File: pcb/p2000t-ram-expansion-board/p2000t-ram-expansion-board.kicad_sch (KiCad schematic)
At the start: 22 parts, among them J1 EXTENSION BOARD, J2 POWER, U1 74HC04, U10 74HC32, U2 CY62256-70PC, U3 74HC32, U4 CY62256-70PC, U5 74HC688, U6 74HC04, U7 74HC08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

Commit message: Revising design
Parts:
- removed C10: 0.1uF, symbol Device:C
- removed U1, U6: 74HC04, Package_DIP:DIP-14_W7.62mm_Socket, symbol 74xx:74HC04
- removed U10, U3: 74HC32, Package_DIP:DIP-14_W7.62mm_Socket, symbol 74xx:74LS32
- removed U7, U9: 74HC08, Package_DIP:DIP-14_W7.62mm_Socket, symbol 74xx:74LS08
- added U2, U5: 74HC00, Package_DIP:DIP-14_W7.62mm_Socket, symbol 74xx:74HC00
- added U6: 74HC32, Package_DIP:DIP-14_W7.62mm_Socket, symbol 74xx:74LS32
- added U8: 74LHC157, Package_DIP:DIP-16_W7.62mm_Socket, symbol 74xx:74LS157
- C1, C2, C6: footprint (none) -> Capacitor_THT:C_Disc_D5.0mm_W2.5mm_P5.00mm
- C3: renamed from C9; footprint (none) -> Capacitor_THT:C_Disc_D5.0mm_W2.5mm_P5.00mm
- C4: renamed from C3; footprint (none) -> Capacitor_THT:CP_Radial_D6.3mm_P2.50mm
- C5: renamed from C4; footprint (none) -> Capacitor_THT:C_Disc_D5.0mm_W2.5mm_P5.00mm
- C7: renamed from C8; footprint (none) -> Capacitor_THT:C_Disc_D5.0mm_W2.5mm_P5.00mm
- C8: renamed from C5; footprint (none) -> Capacitor_THT:C_Disc_D5.0mm_W2.5mm_P5.00mm
- C9: renamed from C7; footprint (none) -> Capacitor_THT:C_Disc_D5.0mm_W2.5mm_P5.00mm
- J1: value EXTENSION BOARD -> EXPANSION BOARD; footprint Connector_PinSocket_2.54mm:PinSocket_2x20_P2.54mm_Horizontal -> Connector_PinHeader_2.54mm:PinHeader_2x20_P2.54mm_Horizontal
- J2: footprint (none) -> Connector_PinHeader_2.54mm:PinHeader_1x02_P2.54mm_Vertical
- renumbered U2 to U1, U4 to U3, U5 to U4, U8 to U7
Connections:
- net +5V: now also U2.14 (VCC), U5.14 (VCC), U6.14 (VCC), U8.16 (VCC), U8.6 (I1b)
- net A0: now also J1.12 (Pin_12); no longer J1.11 (Pin_11)
- net A1: now also J1.11 (Pin_11); no longer J1.12 (Pin_12)
- net A10: now also J1.22 (Pin_22); no longer J1.21 (Pin_21)
- net A11: now also J1.21 (Pin_21); no longer J1.22 (Pin_22)
- net A12: now also J1.24 (Pin_24); no longer J1.23 (Pin_23)
- net A13: now also J1.23 (Pin_23), U8.2 (I0a); no longer J1.24 (Pin_24)
- net A14: now also J1.26 (Pin_26), U5.10, U5.2, U5.9, U8.1 (S); no longer J1.25 (Pin_25)
- net A2: now also J1.14 (Pin_14); no longer J1.13 (Pin_13)
- net A3: now also J1.13 (Pin_13); no longer J1.14 (Pin_14)
- net A4: now also J1.16 (Pin_16); no longer J1.15 (Pin_15)
- net A5: now also J1.15 (Pin_15); no longer J1.16 (Pin_16)
- net A6: now also J1.18 (Pin_18); no longer J1.17 (Pin_17)
- net A7: now also J1.17 (Pin_17); no longer J1.18 (Pin_18)
- net A8: now also J1.20 (Pin_20); no longer J1.19 (Pin_19)
- net A9: now also J1.19 (Pin_19); no longer J1.20 (Pin_20)
- net D0: now also J1.4 (Pin_4); no longer J1.3 (Pin_3)
- net D1: now also J1.3 (Pin_3); no longer J1.4 (Pin_4)
- net D2: now also J1.6 (Pin_6); no longer J1.5 (Pin_5)
- net D3: now also J1.5 (Pin_5), U7.11 (D3); no longer J1.6 (Pin_6)
- net D4: now also J1.8 (Pin_8); no longer J1.7 (Pin_7)
- net D5: now also J1.7 (Pin_7); no longer J1.8 (Pin_8)
- net D6: now also J1.10 (Pin_10); no longer J1.9 (Pin_9)
- net D7: now also J1.9 (Pin_9); no longer J1.10 (Pin_10)
- net GND: now also J1.2 (Pin_2), U2.7 (GND), U5.7 (GND), U6.7 (GND), U8.15 (E), U8.5 (I0b), U8.8 (GND); no longer U7.11 (D3)
- net RAMS2: now also J1.25 (Pin_25), U2.13; no longer J1.26 (Pin_26)
- net S0: now also U8.10 (I1c), U8.11 (I0c), U8.3 (I1a)
- net S1: now also U6.9
- net S2: now also U6.10, U8.13 (I1d), U8.14 (I0d)
- net ~{CS1}: now also U1.20 (~{CS}), U6.11
- net ~{IORQ}: now also J1.32 (Pin_32); no longer J1.31 (Pin_31)
- net ~{MRQ}: now also J1.28 (Pin_28), U2.10, U2.9; no longer J1.27 (Pin_27)
- net ~{RD}: now also J1.27 (Pin_27); no longer J1.28 (Pin_28)
- net ~{RES}: now also J1.33 (Pin_33), U2.1, U2.2; no longer J1.34 (Pin_34)
- net ~{WR}: now also J1.29 (Pin_29), U2.4, U2.5; no longer J1.30 (Pin_30)
- net ~{CS2}: now reaches U3.20 (~{CS})
- net ~{CS2}: now also U6.3
- net WR: now reaches U7.7 (Cp)
- net WR: now also U2.6
- net RES: now reaches U7.15 (Mr)
- net RES: now also U2.3
- net A13P renamed A13_1
- net A13_1: now also U8.4 (Za); no longer U3.26 (A13)
- net A14P renamed A14_1
- net A14_1: now also U8.7 (Zb); no longer U3.1 (A14)
- new net: U2.12, U2.8
- new net: U5.1, U5.4, U5.5, U6.8
- new net: U5.6, U6.4
- new net: U5.11, U6.12
- new net: U5.8, U6.5
- new net: U5.12, U5.13, U6.6
- new net: U5.3, U6.1
- new net A13_2: U3.26 (A13), U8.9 (Zc)
- new net A14_2: U3.1 (A14), U8.12 (Zd)
- new net ~{REN}: U2.11, U6.13, U6.2
- no-connect marks 15 -> 11
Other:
- note added: "Truth table CS1\ CS2\ A13 A14 S0 S1 S2 A13_1 A14_1 A13_2 A14_2 0 1 0 0 x x x 0 0 x x 0 1 1 0 x x x 1 0 x x 0 1 x 1 0 x x 0 1 x x #00 0 1 x 1 1 x x 1 1 x x #01 1 0 x 1 0 1 0 x x 0 0 #02 1 0 x 1 1 1 0 x x 1 0 #03 1 0 x 1 0 0 1 x x 0 1 #04 1 0 x 1 1 0 1 x x 1 1 #05"
- note added: "Whether one of the two RAM chips should be set active"
- note removed: "L"
- moved on the sheet: C1, C2, C3, C4, C5, C6, C7, C9, J2, U1, U3

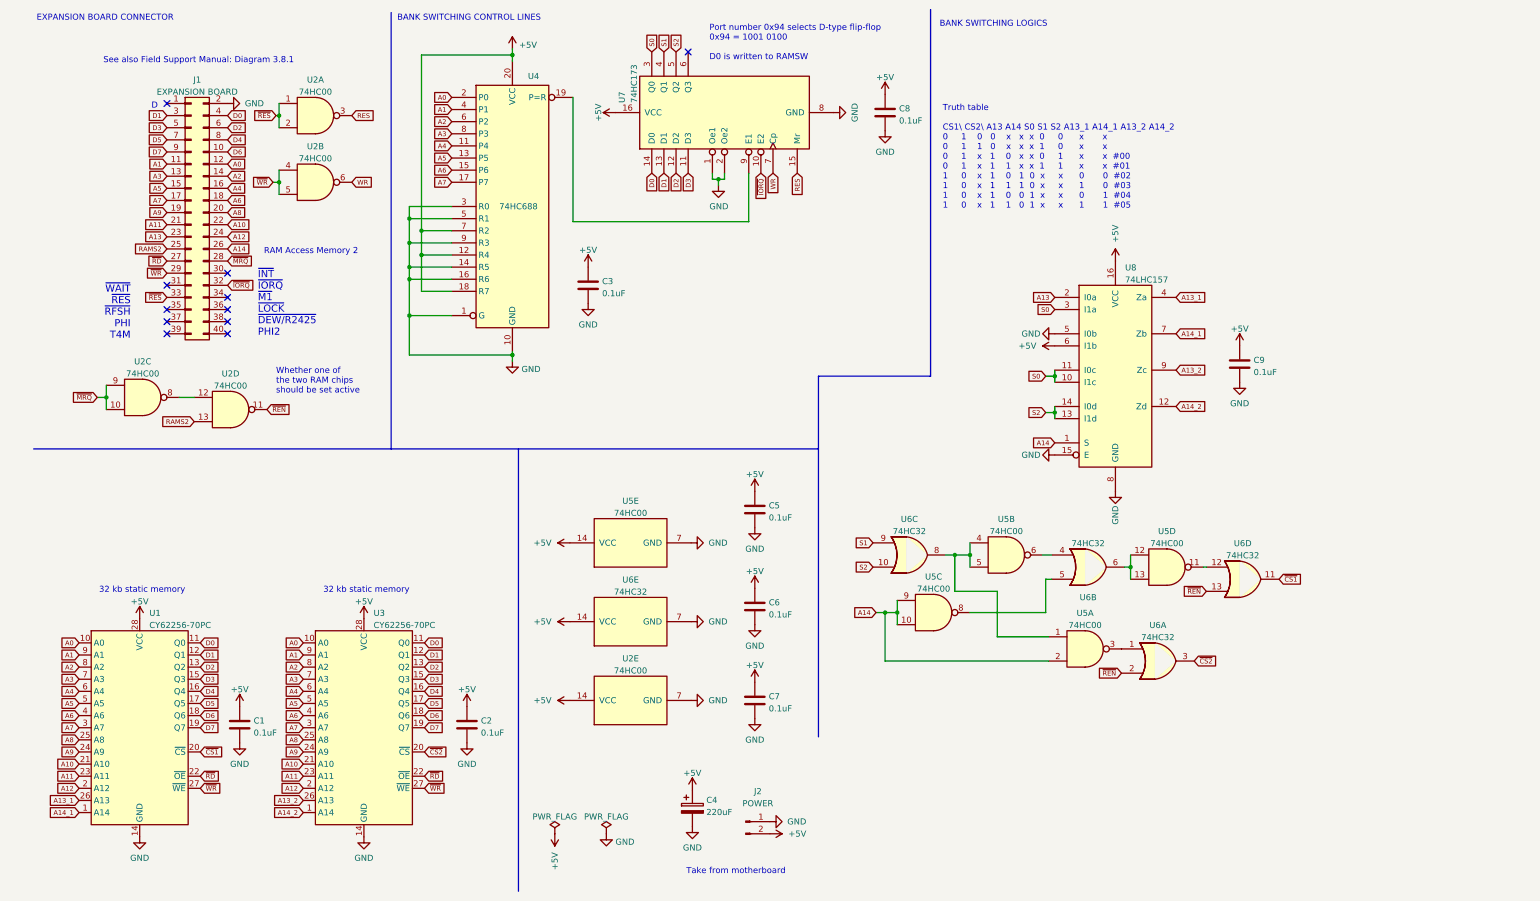
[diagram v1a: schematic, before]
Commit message: Adding reverse polarity diode and silk screen comments
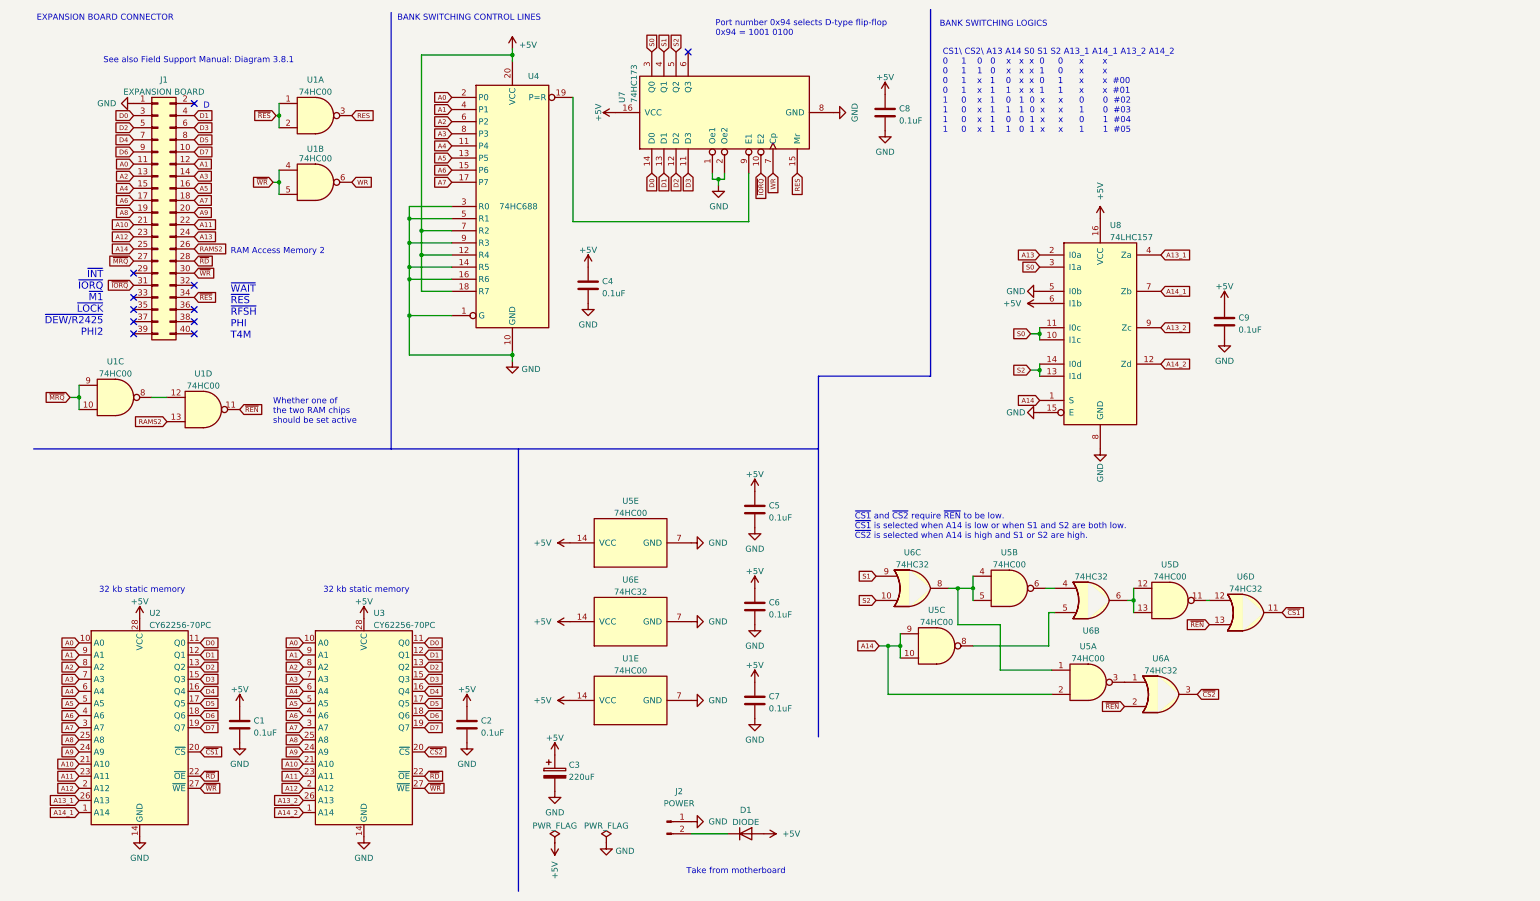
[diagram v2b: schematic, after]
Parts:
- added D1: DIODE, Diode_THT:D_DO-35_SOD27_P7.62mm_Horizontal, symbol Simulation_SPICE:DIODE
- J1: footprint Connector_PinHeader_2.54mm:PinHeader_2x20_P2.54mm_Horizontal -> Connector_PinHeader_2.54mm:PinHeader_2x20_P2.54mm_Vertical
- U2: renamed from U1; footprint Package_DIP:DIP-28_W15.24mm -> Package_DIP:DIP-28_W15.24mm_Socket
- U3: footprint Package_DIP:DIP-28_W15.24mm -> Package_DIP:DIP-28_W15.24mm_Socket
- renumbered C4 to C3, C3 to C4, U2 to U1
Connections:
- net +5V: now also D1.1 (A); no longer J2.2 (Pin_2)
- net A0: now also J1.11 (Pin_11); no longer J1.12 (Pin_12)
- net A1: now also J1.12 (Pin_12); no longer J1.11 (Pin_11)
- net A10: now also J1.21 (Pin_21); no longer J1.22 (Pin_22)
- net A11: now also J1.22 (Pin_22); no longer J1.21 (Pin_21)
- net A12: now also J1.23 (Pin_23); no longer J1.24 (Pin_24)
- net A13: now also J1.24 (Pin_24); no longer J1.23 (Pin_23)
- net A14: now also J1.25 (Pin_25); no longer J1.26 (Pin_26)
- net A2: now also J1.13 (Pin_13); no longer J1.14 (Pin_14)
- net A3: now also J1.14 (Pin_14); no longer J1.13 (Pin_13)
- net A4: now also J1.15 (Pin_15); no longer J1.16 (Pin_16)
- net A5: now also J1.16 (Pin_16); no longer J1.15 (Pin_15)
- net A6: now also J1.17 (Pin_17); no longer J1.18 (Pin_18)
- net A7: now also J1.18 (Pin_18); no longer J1.17 (Pin_17)
- net A8: now also J1.19 (Pin_19); no longer J1.20 (Pin_20)
- net A9: now also J1.20 (Pin_20); no longer J1.19 (Pin_19)
- net D0: now also J1.3 (Pin_3); no longer J1.4 (Pin_4)
- net D1: now also J1.4 (Pin_4); no longer J1.3 (Pin_3)
- net D2: now also J1.5 (Pin_5); no longer J1.6 (Pin_6)
- net D3: now also J1.6 (Pin_6); no longer J1.5 (Pin_5)
- net D4: now also J1.7 (Pin_7); no longer J1.8 (Pin_8)
- net D5: now also J1.8 (Pin_8); no longer J1.7 (Pin_7)
- net D6: now also J1.9 (Pin_9); no longer J1.10 (Pin_10)
- net D7: now also J1.10 (Pin_10); no longer J1.9 (Pin_9)
- net GND: now also J1.1 (Pin_1); no longer J1.2 (Pin_2)
- net RAMS2: now also J1.26 (Pin_26); no longer J1.25 (Pin_25)
- net ~{IORQ}: now also J1.31 (Pin_31); no longer J1.32 (Pin_32)
- net ~{MRQ}: now also J1.27 (Pin_27); no longer J1.28 (Pin_28)
- net ~{RD}: now also J1.28 (Pin_28); no longer J1.27 (Pin_27)
- net ~{RES}: now also J1.34 (Pin_34); no longer J1.33 (Pin_33)
- net ~{WR}: now also J1.30 (Pin_30); no longer J1.29 (Pin_29)
- new net: D1.2 (K), J2.2 (Pin_2)
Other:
- note added: "CS1\ CS2\ A13 A14 S0 S1 S2 A13_1 A14_1 A13_2 A14_2 0 1 0 0 x x x 0 0 x x 0 1 1 0 x x x 1 0 x x 0 1 x 1 0 x x 0 1 x x #00 0 1 x 1 1 x x 1 1 x x #01 1 0 x 1 0 1 0 x x 0 0 #02 1 0 x 1 1 1 0 x x 1 0 #03 1 0 x 1 0 0 1 x x 0 1 #04 1 0 x 1 1 0 1 x x 1 1 #05"
- note added: "Port number 0x94 selects D-type flip-flop 0x94 = 1001 0100"
- note added: "~{CS1} and ~{CS2} require ~{REN} to be low. ~{CS1} is selected when A14 is low or when S1 and S2 are both low. ~{CS2} is selected when A14 is high and S1 or S2 are high."
- note removed: "Port number 0x94 selects D-type flip-flop 0x94 = 1001 0100 D0 is written to RAMSW"
- note removed: "Truth table CS1\ CS2\ A13 A14 S0 S1 S2 A13_1 A14_1 A13_2 A14_2 0 1 0 0 x x x 0 0 x x 0 1 1 0 x x x 1 0 x x 0 1 x 1 0 x x 0 1 x x #00 0 1 x 1 1 x x 1 1 x x #01 1 0 x 1 0 1 0 x x 0 0 #02 1 0 x 1 1 1 0 x x 1 0 #03 1 0 x 1 0 0 1 x x 0 1 #04 1 0 x 1 1 0 1 x x 1 1 #05"
- moved on the sheet: C3, C9, J1, J2, U1C, U1D, U5A, U5B, U5C, U5D, U6A, U6B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

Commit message: Improving layout
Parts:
- removed D1: DIODE, Diode_THT:D_DO-35_SOD27_P7.62mm_Horizontal, symbol Simulation_SPICE:DIODE
- removed U1: 74HC00, Package_DIP:DIP-14_W7.62mm_Socket, symbol 74xx:74HC00
- added D1: DIODE, Diode_THT:D_DO-35_SOD27_P7.62mm_Horizontal, symbol Device:D
- added U1: 74HC04, Package_DIP:DIP-14_W7.62mm_Socket, symbol 74xx:74HC04
- renumbered U5 to U3, U3 to U4, U4 to U5
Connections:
- net +5V: now also D1.1 (K), U1.14 (VCC)
- net A13: now also U3.9; no longer U8.2 (I0a)
- net A14: now also U8.2 (I0a); no longer U3.2, U3.9, U8.1 (S)
- net GND: now also U6.4, U6.5, U1.7 (GND), U1.9
- net RAMS2: now also U3.13
- net RES: now also U1.2
- net WR: now also U1.4
- net ~{MRQ}: now also U1.13
- net ~{REN}: now also U3.11
- net ~{RES}: now also U1.1
- net ~{WR}: now also U1.3
- net S1 | S2: now reaches U3.1, U3.5, U6.8
- net S1 | S2: no longer U3.4
- net at U3.6: now also U6.1; no longer U6.4
- net at U6.12: now also U1.10; no longer U3.11
- net at U3.8: now also U1.5; no longer U6.5
- net VCC: now reaches J2.2 (Pin_2)
- net VCC: now also D1.2 (A)
- net at U3.3: now also U1.11; no longer U6.1
- new net: U1.12, U3.12
- new net BR: U1.6, U3.2, U3.4, U8.1 (S)
- now unconnected: U6.6
- no-connect marks 11 -> 13
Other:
- note added: "BR: address $E000-$FFFF"
- note added: "CHIP2"
- note added: "E000-FFFF"
- note added: "VIN"
- note added: "VOUT"
- note removed: "CS1\ CS2\ A13 A14 S0 S1 S2 A13_1 A14_1 A13_2 A14_2 0 1 0 0 x x x 0 0 x x 0 1 1 0 x x x 1 0 x x 0 1 x 1 0 x x 0 1 x x #00 0 1 x 1 1 x x 1 1 x x #01 1 0 x 1 0 1 0 x x 0 0 #02 1 0 x 1 1 1 0 x x 1 0 #03 1 0 x 1 0 0 1 x x 0 1 #04 1 0 x 1 1 0 1 x x 1 1 #05"
- note removed: "Take from motherboard"
- note removed: "~{CS1} and ~{CS2} require ~{REN} to be low. ~{CS1} is selected when A14 is low or when S1 and S2 are both low. ~{CS2} is selected when A14 is high and S1 or S2 are high."
- moved on the sheet: C9, J2, U3A, U3B, U3C, U3D, U6A, U6B, U6C, U6D, U8

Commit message: Adding GERBERS
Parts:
- added J?: TERMINAL, symbol Connector:Screw_Terminal_01x02
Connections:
- net A14: no longer U8.2 (I0a)
- net BR: now also U1.11, U3.3, U6.1; no longer U1.6, U3.2, U3.4
- net GND: now also U3.4, U3.5, U8.2 (I0a), J?.1 (Pin_1)
- net VCC: now also J?.2 (Pin_2)
- net at U3.6: no longer U6.1
- net S1 | S2: no longer names the net of U3.1, U6.8
- net S1 | S2: no longer U3.5
- new net: U1.6, U3.2
- no-connect marks 13 -> 14
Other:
- note removed: "CHIP2"
- moved on the sheet: D1, J2, U1E, U3B, U6D

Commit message: Adding ramtest script
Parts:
- U8: value 74LHC157 -> 74HC157
- gave numbers to parts that had none: 1
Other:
- note added: "Address is at least 0xE000, then both A13 and A14 are high"
- note added: "Chip1?"
- note removed: "E000-FFFF"

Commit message: Revising PCB and updating code
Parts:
- added D2, D3, D4: LED, LED_SMD:LED_0805_2012Metric_Pad1.15x1.40mm_HandSolder, symbol Device:LED
- added R1, R2, R3: R, Resistor_SMD:R_0805_2012Metric_Pad1.20x1.40mm_HandSolder, symbol Device:R
- J3: footprint (none) -> TerminalBlock:TerminalBlock_bornier-2_P5.08mm
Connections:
- net GND: now also U7.10 (E2), U7.9 (E1), D2.1 (K), D3.1 (K), D4.1 (K); no longer U5.1 (G), U6.4, U6.5
- net S0: now also R1.1
- net S1: now also R2.1
- net S2: now also R3.1
- net ~{IORQ}: now also U5.1 (G); no longer U7.10 (E2)
- net ~{WR}: now also U6.5; no longer U1.3
- net at U6.6: now also U1.3
- net at U5.19 (P=R): now also U6.4; no longer U7.9 (E1)
- net EO: now reaches U1.6, U3.2
- net EO: now also U8.1 (S)
- net BR: no longer names the net of U1.11, U3.3, U6.1
- net BR: no longer U8.1 (S)
- net WR: no longer names the net of U1.4, U7.7 (Cp)
- new net: D2.2 (A), R1.2
- new net: D4.2 (A), R3.2
- new net: D3.2 (A), R2.2
- no-connect marks 14 -> 13
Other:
- note added: "Bank LEDS (for debugging purposes)"
- note added: "Unused gates tied to GND"
- moved on the sheet: U1B, U1D, U3B, U6B

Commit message: Polishing PCB
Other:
- note added: "0x94"
- note added: "A13_2 and A14_2 can be directly tied to S0 and S2, but this set-up gives buffering."
- note added: "Active high reset needed for 74HC173"
- note added: "Because of timing contraints, ~{WR} needs to be combined with ~{P=Q}"
- note added: "Chip select circuitry"
- note added: "Only active on ~{IORQ}"
- note added: "Power lines"
- note added: "RAM CHIPS"
- note added: "address in E000-FFFF?"
- note removed: "BR: address $E000-$FFFF"
- note removed: "Chip1?"
- moved on the sheet: C1, C2, U2, U4

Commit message: Adding 74HC245
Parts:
- removed D2, D3, D4: LED, LED_SMD:LED_0805_2012Metric_Pad1.15x1.40mm_HandSolder, symbol Device:LED
- removed R1, R2, R3: R, Resistor_SMD:R_0805_2012Metric_Pad1.20x1.40mm_HandSolder, symbol Device:R
- added C9: 0.1uF, Capacitor_THT:C_Disc_D5.0mm_W2.5mm_P5.00mm, symbol Device:C
- added U8: 74HC245, Package_DIP:DIP-20_W7.62mm_Socket, symbol 74xx:74LS245
- renumbered C9 to C10, U8 to U9
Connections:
- net +5V: now also C9.1, U8.1 (A->B), U8.20 (VCC)
- net D0: now also U8.18 (B0)
- net D1: now also U8.17 (B1)
- net D2: now also U8.16 (B2)
- net D3: now also U8.15 (B3)
- net D4: now also U8.14 (B4)
- net D5: now also U8.13 (B5)
- net D6: now also U8.12 (B6)
- net D7: now also U8.11 (B7)
- net GND: now also C9.2, U8.10 (GND), U8.6 (A4), U8.7 (A5), U8.8 (A6), U8.9 (A7); no longer U3.4, U3.5
- net S0: now also U8.2 (A0)
- net S1: now also U8.3 (A1)
- net S2: now also U8.4 (A2)
- net ~{CS1}: now also U3.6; no longer U6.11
- net ~{RD}: now also U6.12
- net ~{REN}: now also U1.11; no longer U6.13
- net at U1.10: now also U3.5; no longer U6.12
- net ~{P=Q}: now reaches U5.19 (P=R), U6.4
- net ~{P=Q}: now also U6.13
- net S3: now reaches U7.6 (Q3)
- net S3: now also U8.5 (A3)
- net at U3.3, U6.1: now also U3.4; no longer U1.11
- new net: U6.11, U8.19 (CE)
- no-connect marks 13 -> 12
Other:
- note added: "ADDR >= 0xE000, then both A13 and A14 are high"
- note added: "~(S1 | S2) | ~(A13 & A14)"
- note added: "~{(S1 | S2) & (A13 & A14)}"
- note removed: "Address is at least 0xE000, then both A13 and A14 are high"
- note removed: "Bank LEDS (for debugging purposes)"
- note removed: "Unused gates tied to GND"
- moved on the sheet: U1C, U1D, U1E, U3A, U3B, U3C, U6A, U6C, U6D
